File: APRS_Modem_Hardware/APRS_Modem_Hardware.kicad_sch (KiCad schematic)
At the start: 29 parts, among them Q1 2N3904, U1 LM741

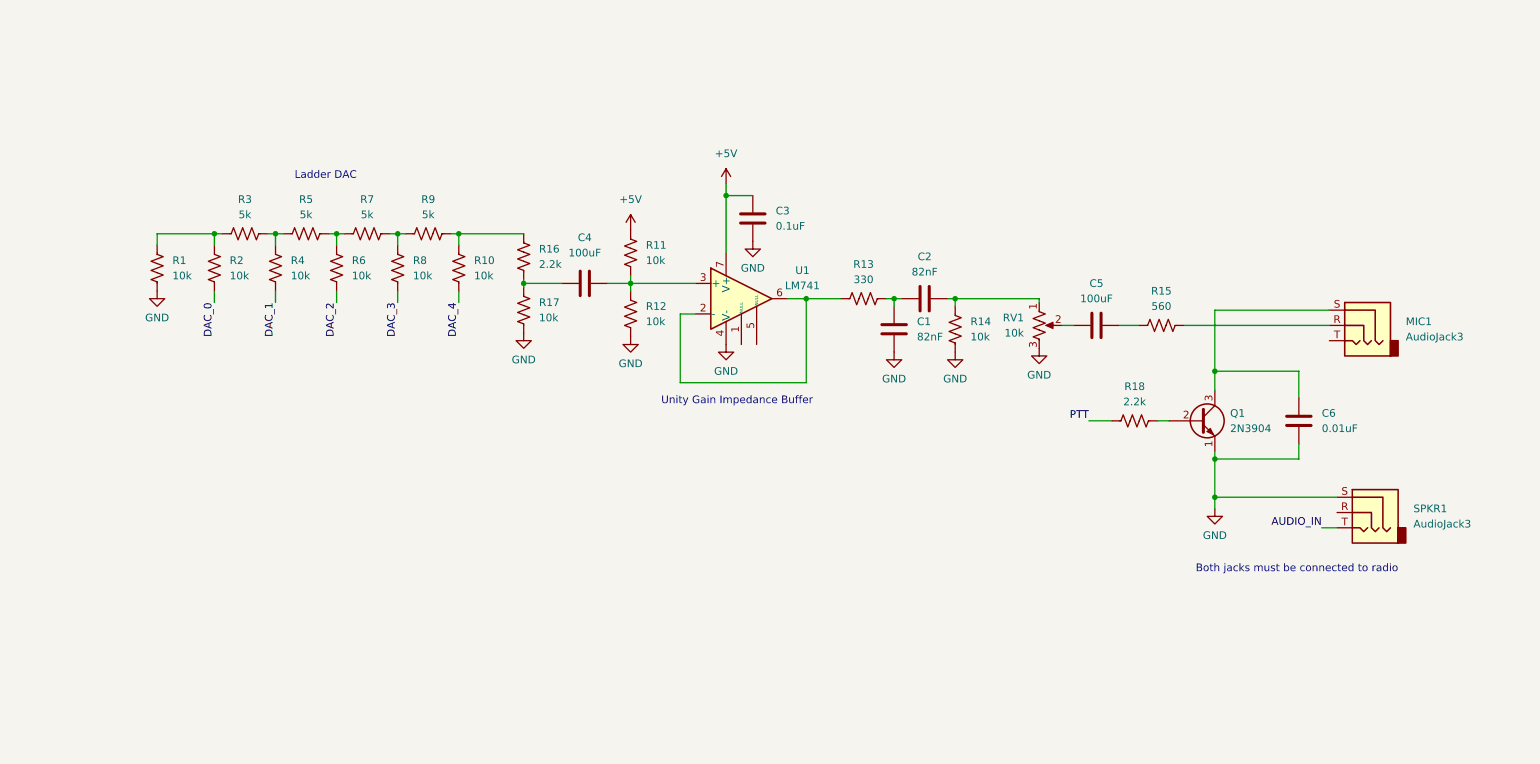
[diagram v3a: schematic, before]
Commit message: update schematic
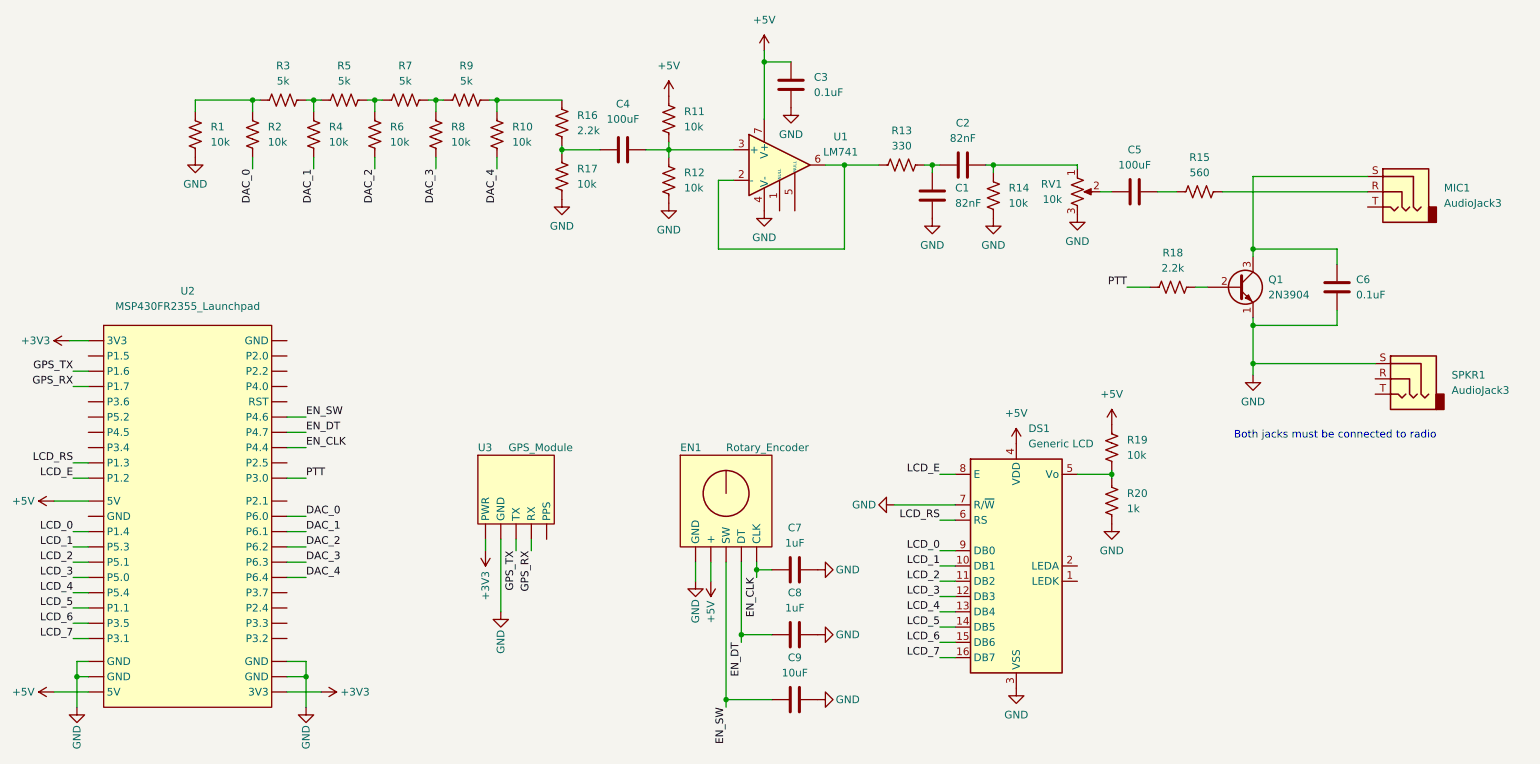
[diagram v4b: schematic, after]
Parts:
- added C7, C8: 1uF, symbol Device:C
- added C9: 10uF, symbol Device:C
- added DS1: Generic LCD, Display:HY1602E, symbol Display_Character:HY1602E
- added EN1: Rotary_Encoder, symbol APRS_Modem_Parts:Rotary_Encoder
- added R19: 10k, symbol Device:R_US
- added R20: 1k, symbol Device:R_US
- added U2: MSP430FR2355_Launchpad, symbol APRS_Modem_Parts:MSP430FR2355_Launchpad
- added U3: GPS_Module, symbol APRS_Modem_Parts:GPS_Module
- C6: value 0.01uF -> 0.1uF
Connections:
- net +5V: now also DS1.4 (VDD), EN1. (SW), R19.1, U2. (RST)
- net DAC_0: now also U2. (RST)
- net DAC_1: now also U2. (RST)
- net DAC_2: now also U2. (RST)
- net DAC_3: now also U2. (RST)
- net DAC_4: now also U2. (RST)
- net GND: now also C7.2, C8.2, C9.2, DS1.3 (VSS), DS1.7 (R/~{W}), EN1. (SW), R20.2, U2. (RST), U3. (TX)
- net PTT: now also U2. (RST)
- net AUDIO_IN: no longer names the net of SPKR1.T
- new net: DS1.5 (Vo), R19.2, R20.1
- new net +3V3: U2. (RST), U3. (TX)
- new net EN_CLK: C7.1, EN1. (SW), U2. (RST)
- new net EN_DT: C8.1, EN1. (SW), U2. (RST)
- new net EN_SW: C9.1, EN1. (SW), U2. (RST)
- new net GPS_RX: U2. (RST), U3. (TX)
- new net GPS_TX: U2. (RST), U3. (TX)
- new net LCD_0: DS1.9 (DB0), U2. (RST)
- new net LCD_1: DS1.10 (DB1), U2. (RST)
- new net LCD_2: DS1.11 (DB2), U2. (RST)
- new net LCD_3: DS1.12 (DB3), U2. (RST)
- new net LCD_4: DS1.13 (DB4), U2. (RST)
- new net LCD_5: DS1.14 (DB5), U2. (RST)
- new net LCD_6: DS1.15 (DB6), U2. (RST)
- new net LCD_7: DS1.16 (DB7), U2. (RST)
- new net LCD_E: DS1.8 (E), U2. (RST)
- new net LCD_RS: DS1.6 (RS), U2. (RST)
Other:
- note removed: "Ladder DAC"
- note removed: "Unity Gain Impedance Buffer"
- moved on the sheet: C1, C2, C3, C4, C5, C6, MIC1, Q1, R1, R10, R11, R12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
